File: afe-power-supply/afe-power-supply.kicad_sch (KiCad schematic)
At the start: 14 parts, among them J1 Screw_Terminal_01x03, J2 Screw_Terminal_01x02, J3 Conn_01x01, U1 Generic_DIP24_Dual_Isolated_D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

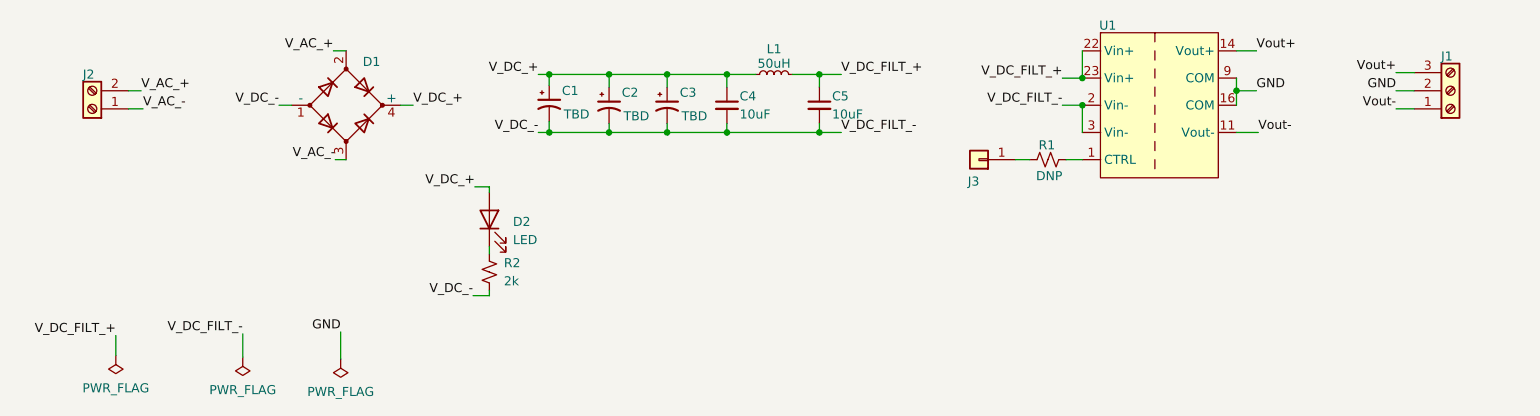
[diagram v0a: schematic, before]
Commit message: Added fuse and generated gerber files for afe power supply
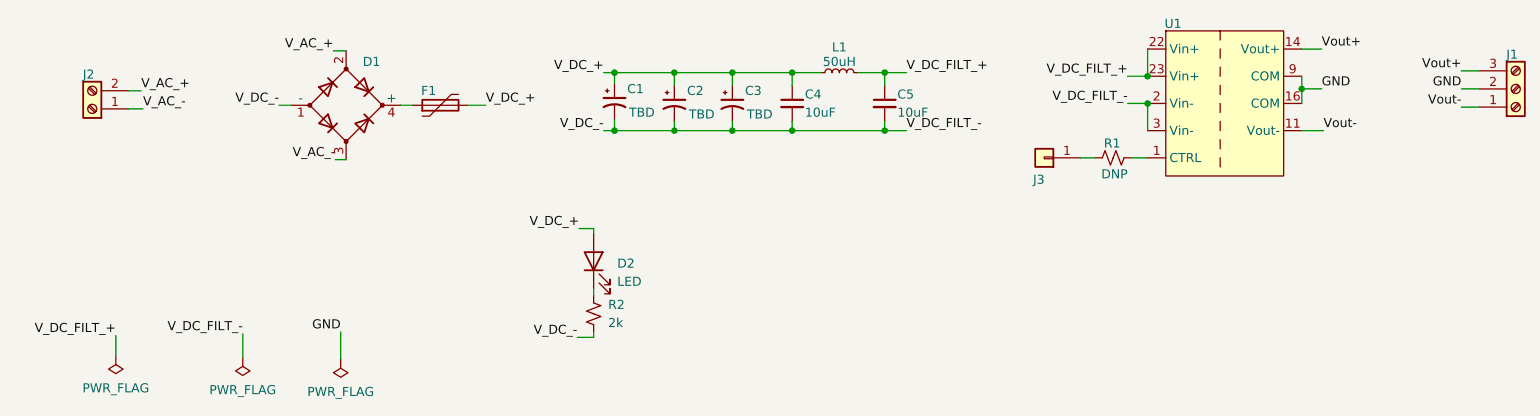
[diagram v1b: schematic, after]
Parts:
- added F1: Polyfuse, Resistor_SMD:R_1210_3225Metric_Pad1.30x2.65mm_HandSolder, symbol Device:Polyfuse
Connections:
- net V_DC_+: now also F1.2; no longer D1.4 (+)
- new net: D1.4 (+), F1.1
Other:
- moved on the sheet: C1, C2, C3, C4, C5, D2, J1, J3, L1, R1, R2, U1
